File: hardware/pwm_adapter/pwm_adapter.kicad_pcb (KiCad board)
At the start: 2 copper layers, 59 parts, among them J1 WAGO250-204, J10 Conn_01x06_Female, J11 Conn_01x06_Female, J12 Conn_01x06_Female, J13 Conn_01x06_Female, J14 Conn_01x03, J15 Conn_01x06_Female, J16 Conn_01x06_Female, J17 Conn_01x06_Female, J18 Conn_01x06_Female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

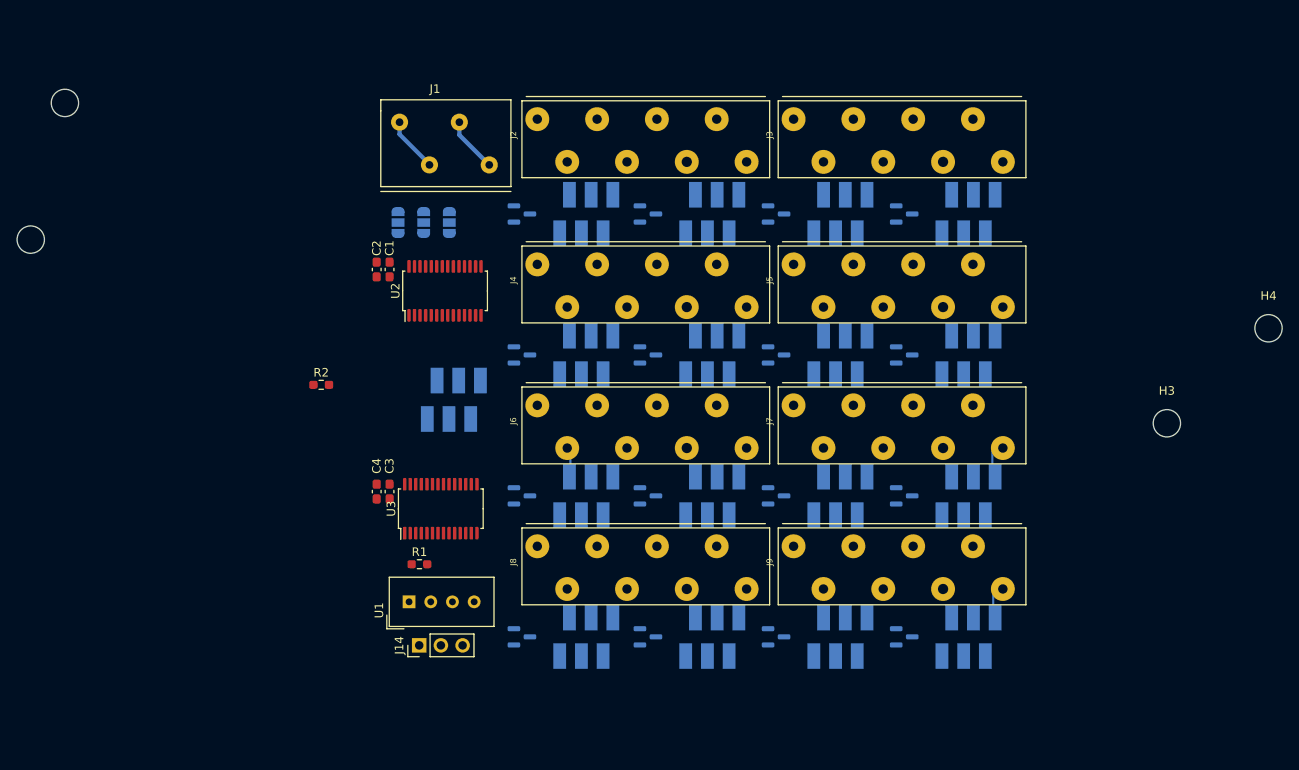
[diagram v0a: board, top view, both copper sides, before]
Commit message: feat: Add fab export options for all pcbs
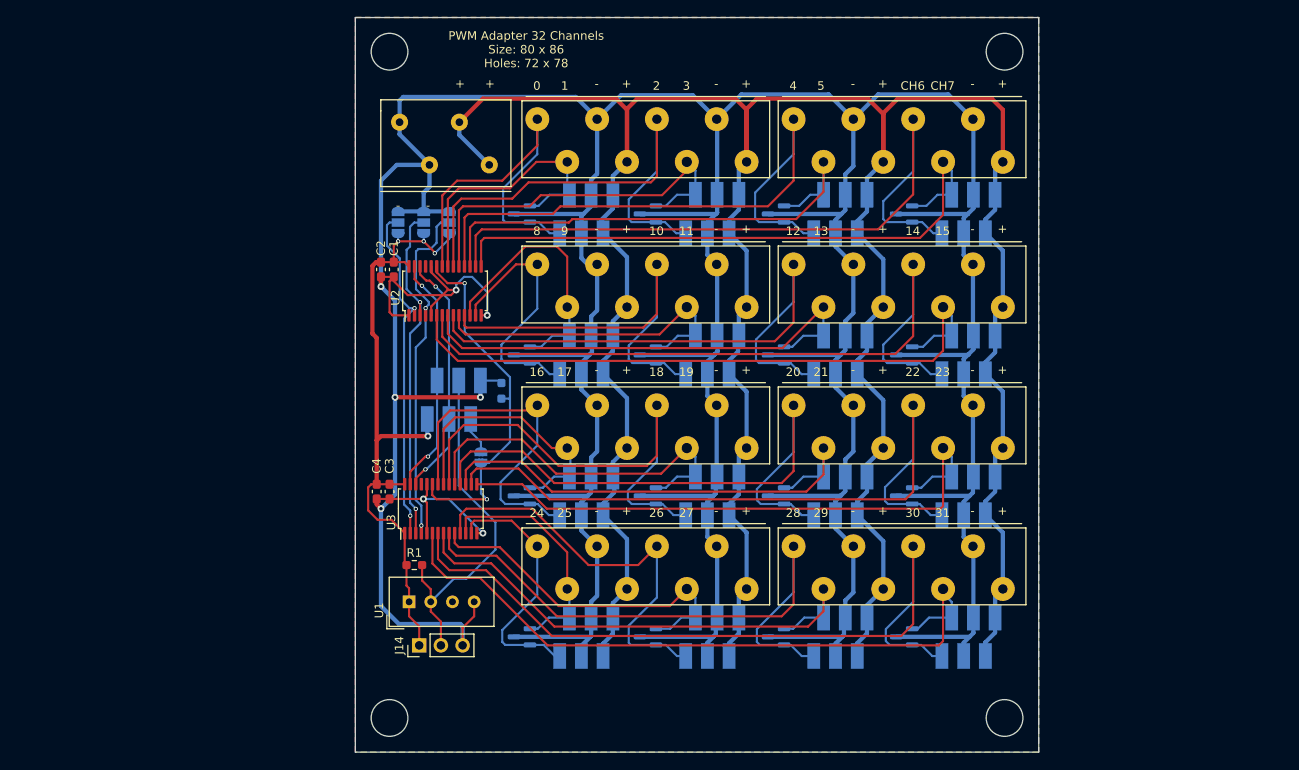
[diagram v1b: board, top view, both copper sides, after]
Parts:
- added JP4: SolderJumper_2_Open, Jumper:SolderJumper-2_P1.3mm_Open_RoundedPad1.0x1.5mm, B.Cu at (39.7, 71.5)
- H1, H2, H3, H4: footprint MountingHole:MountingHole_3.2mm_M3_DIN965 -> MountingHole:MountingHole_4.3mm_M4_DIN965
- R2: moved to B.Cu
- moved H2 116.1 mm to (101.0, 24.0)
- moved H3 97.3 mm to (29.0, 102.0)
- moved H4 55.1 mm to (101.0, 102.0)
- moved H1 38.5 mm to (29.0, 24.0)
- moved R2 21.1 mm to (42.1, 63.7), turned to 90 degrees
- moved R1 0.61 mm to (31.9, 84.1)
- moved C1 0.50 mm to (29.5, 49.5)
- moved C2 0.50 mm to (28.0, 49.5)
- turned D1 to 180 degrees
- turned D10 to 180 degrees
- turned D11 to 180 degrees
- turned D12 to 180 degrees
- turned D13 to 180 degrees
- turned D14 to 180 degrees
- turned D15 to 180 degrees
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- renumbered JP1 to A1, JP2 to A2, JP3 to A3
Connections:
- J10 pad 1: /DIM1 -> /DIM0
- J10 pad 2: /DIM0 -> /DIM1
- J11 pad 1: /DIM3 -> /DIM2
- J11 pad 2: /DIM2 -> /DIM3
- J12 pad 1: /DIM5 -> /DIM4
- J12 pad 2: /DIM4 -> /DIM5
- J13 pad 1: /DIM7 -> /DIM6
- J13 pad 2: /DIM6 -> /DIM7
- J15 pad 1: /DIM9 -> /DIM8
- J15 pad 2: /DIM8 -> /DIM9
- J16 pad 1: /DIM11 -> /DIM10
- J16 pad 2: /DIM10 -> /DIM11
- J17 pad 1: /DIM13 -> /DIM12
- J17 pad 2: /DIM12 -> /DIM13
- J18 pad 1: /DIM15 -> /DIM14
- J18 pad 2: /DIM14 -> /DIM15
- J19 pad 5: /OE -> Net-(J19-Pad5)
- J2 pad 3: +48V -> GND
- J2 pad 4: GND -> +48V
- J2 pad 7: +48V -> GND
- J2 pad 8: GND -> +48V
- J20 pad 1: /DIM17 -> /DIM16
- J20 pad 2: /DIM16 -> /DIM17
- J21 pad 1: /DIM19 -> /DIM18
- J21 pad 2: /DIM18 -> /DIM19
- J22 pad 1: /DIM21 -> /DIM20
- J22 pad 2: /DIM20 -> /DIM21
- J23 pad 1: /DIM23 -> /DIM22
- J23 pad 2: /DIM22 -> /DIM23
- J24 pad 1: /DIM25 -> /DIM24
- J24 pad 2: /DIM24 -> /DIM25
- J25 pad 1: /DIM27 -> /DIM26
- J25 pad 2: /DIM26 -> /DIM27
- J26 pad 1: /DIM29 -> /DIM28
- J26 pad 2: /DIM28 -> /DIM29
- J27 pad 1: /DIM31 -> /DIM30
- J27 pad 2: /DIM30 -> /DIM31
- J3 pad 3: +48V -> GND
- J3 pad 4: GND -> +48V
- J3 pad 7: +48V -> GND
- J3 pad 8: GND -> +48V
- J4 pad 3: +48V -> GND
- J4 pad 4: GND -> +48V
- J4 pad 7: +48V -> GND
- J4 pad 8: GND -> +48V
- J5 pad 3: +48V -> GND
- J5 pad 4: GND -> +48V
- J5 pad 7: +48V -> GND
- J5 pad 8: GND -> +48V
- J6 pad 3: +48V -> GND
- J6 pad 4: GND -> +48V
- J6 pad 7: +48V -> GND
- J6 pad 8: GND -> +48V
- J7 pad 3: +48V -> GND
- J7 pad 4: GND -> +48V
- J7 pad 7: +48V -> GND
- J7 pad 8: GND -> +48V
- J8 pad 3: +48V -> GND
- J8 pad 4: GND -> +48V
- J8 pad 7: +48V -> GND
- J8 pad 8: GND -> +48V
- J9 pad 3: +48V -> GND
- J9 pad 4: GND -> +48V
- J9 pad 7: +48V -> GND
- J9 pad 8: GND -> +48V
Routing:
- net GND: track 13.5 -> 653.8 mm, vias 0 -> 8
- net +48V: track 6.45 -> 377.8 mm
- net /DIM30: track 0.00 -> 91.8 mm
- net /DIM14: track 0.00 -> 87.9 mm
- net /DIM6: track 0.00 -> 86.3 mm
- net /DIM22: track 0.00 -> 85.1 mm
- net /DIM31: track 0.00 -> 82.5 mm
- net /DIM15: track 0.00 -> 77.7 mm
- net +3.3V: track 0.00 -> 77.4 mm, vias 0 -> 4
- net /DIM4: track 0.00 -> 74.3 mm
- net /DIM7: track 0.00 -> 73.9 mm
- net /DIM28: track 0.00 -> 73.1 mm
- net /DIM20: track 0.00 -> 72.2 mm
- net /DIM23: track 0.00 -> 71.6 mm
- net /DIM12: track 0.00 -> 70.3 mm
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- added copper zone on B.Cu, net GND
- added copper zone on F.Cu, net GND
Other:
- board outline added: 80 x 86 mm
- board text added: "+"
- board text added: "-"
- board text added: "0"
- board text added: "1"
- board text added: "10"
- board text added: "11"
- board text added: "12"
- board text added: "13"
- board text added: "14"
- board text added: "15"
- board text added: "16"
- board text added: "17"
- board text added: "18"
- board text added: "19"
- board text added: "2"
- board text added: "20"
- board text added: "21"
- board text added: "22"
- board text added: "23"
- board text added: "24"
- board text added: "25"
- board text added: "26"
- board text added: "27"
- board text added: "28"
- board text added: "29"
- board text added: "3"
- board text added: "30"
- board text added: "31"
- board text added: "4"
- board text added: "5"
- board text added: "8"
- board text added: "9"
- board text added: "CH6"
- board text added: "CH7"
- board text added: "PWM Adapter 32 Channels Size: 80 x 86 Holes: 72 x 78"

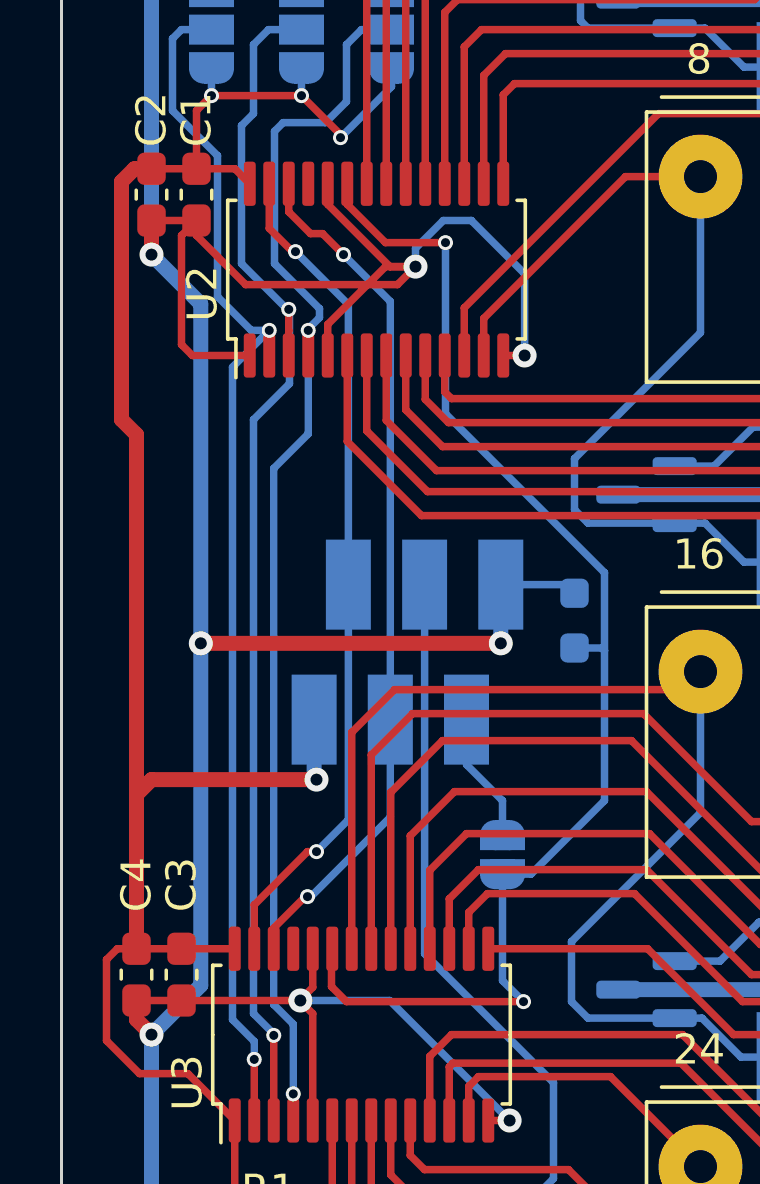
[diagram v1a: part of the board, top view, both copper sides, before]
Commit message: fix: Add GND to ext_clk_in
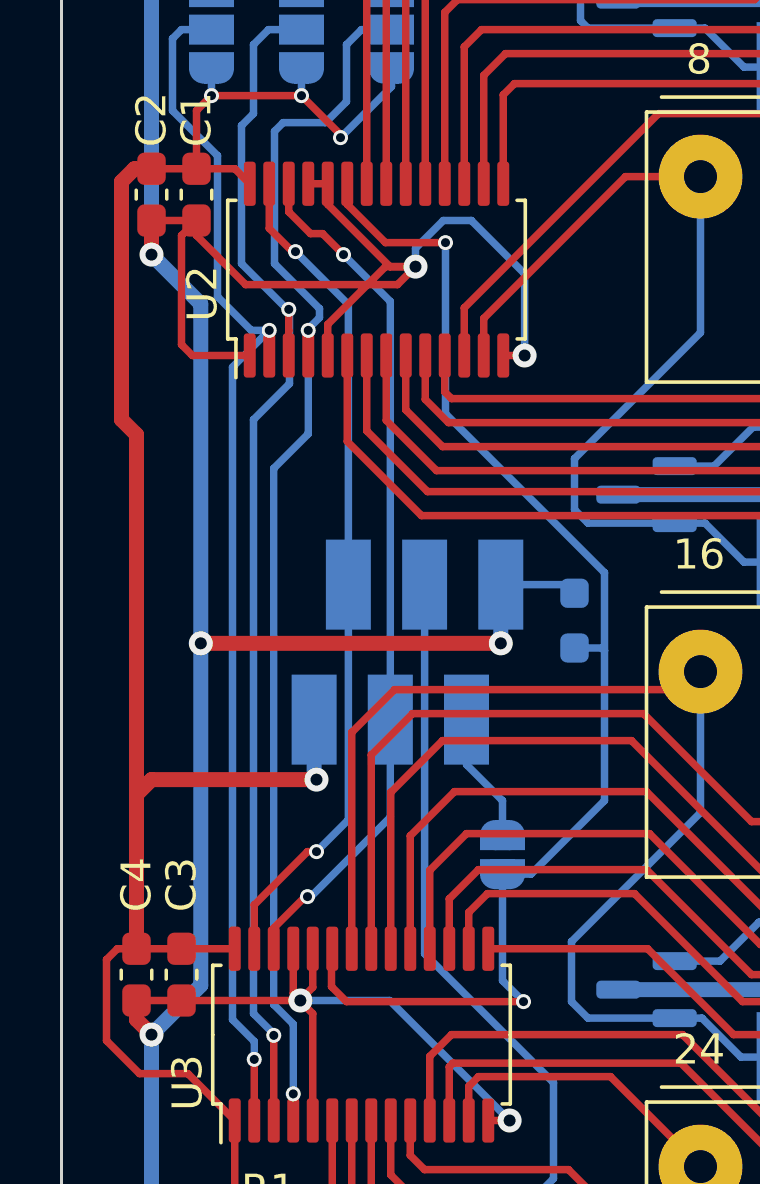
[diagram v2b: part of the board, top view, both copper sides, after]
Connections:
- U2 pad 25: unconnected-(U2-Pad25) -> GND
- U3 pad 25: unconnected-(U3-Pad25) -> GND
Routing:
- net GND: track 653.8 -> 656.3 mm
